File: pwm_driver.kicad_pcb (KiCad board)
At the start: 2 copper layers, 56.6 x 57.7 mm, 40 parts, among them J1 V_{In}, J2 GND_{In}, J3 SolderPad, J4 SolderPad, Q1 BC817, Q2 BC807, Q3 BUK7880-55A, U1 TLV2372, U2 LM393

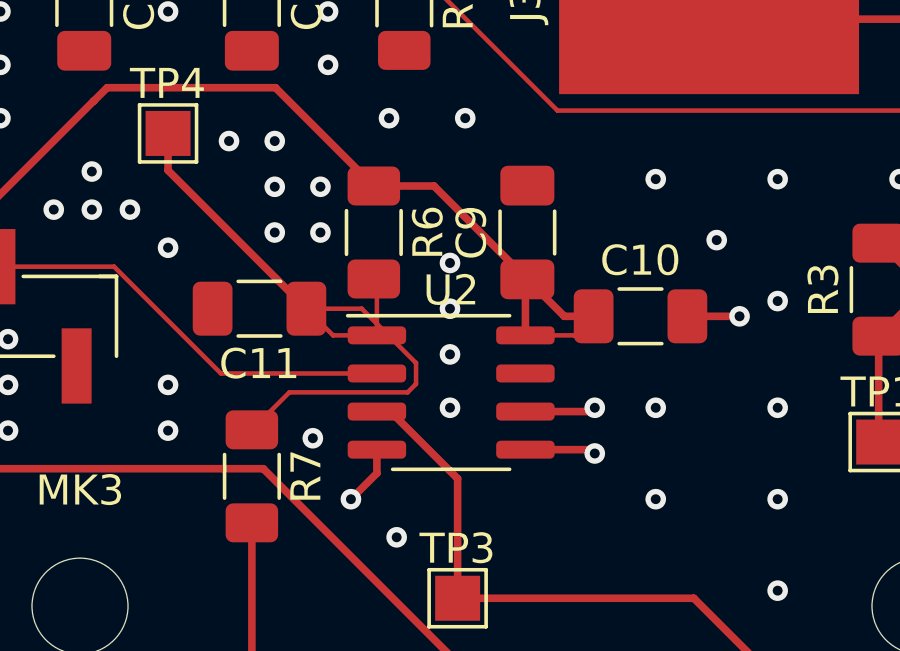
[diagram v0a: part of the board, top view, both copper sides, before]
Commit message: subfolder with simulation model added
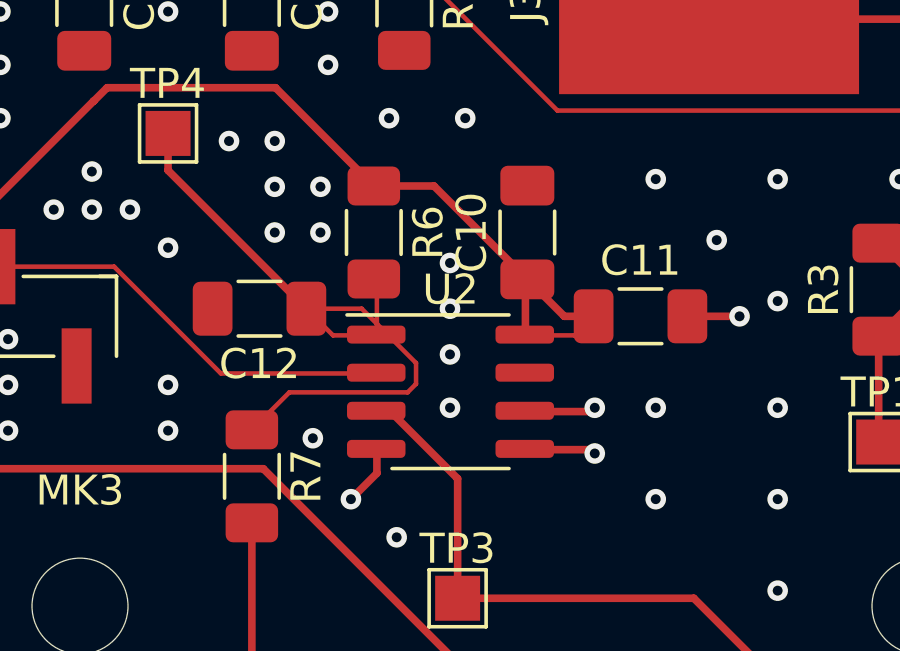
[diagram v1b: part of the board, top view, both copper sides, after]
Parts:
- C1: value 10u -> 33u
- renumbered C9 to C10, C10 to C11, C11 to C12
